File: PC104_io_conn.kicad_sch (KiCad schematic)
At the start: 14 parts, among them J13 ESQ-126-39-G-D_SAI, J15 ESQ-126-39-G-D_SAI

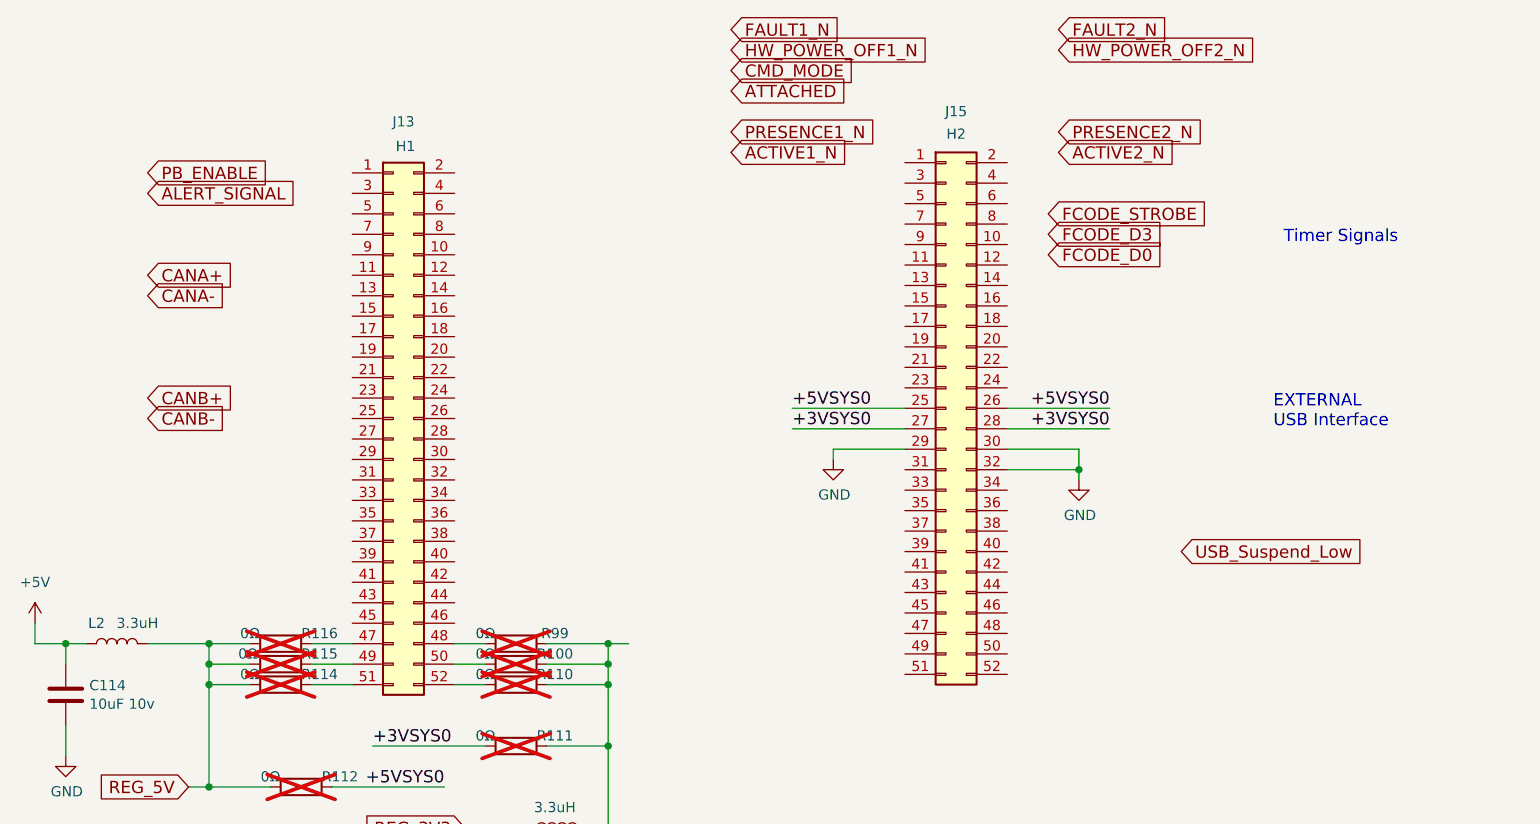
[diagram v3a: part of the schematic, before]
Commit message: Finish up temporary PC104 assignments
Finish up most of what is required for the CubeSat Kit Bus conversion.

Signed-off-by: Corey Minyard <corey@minyard.net>
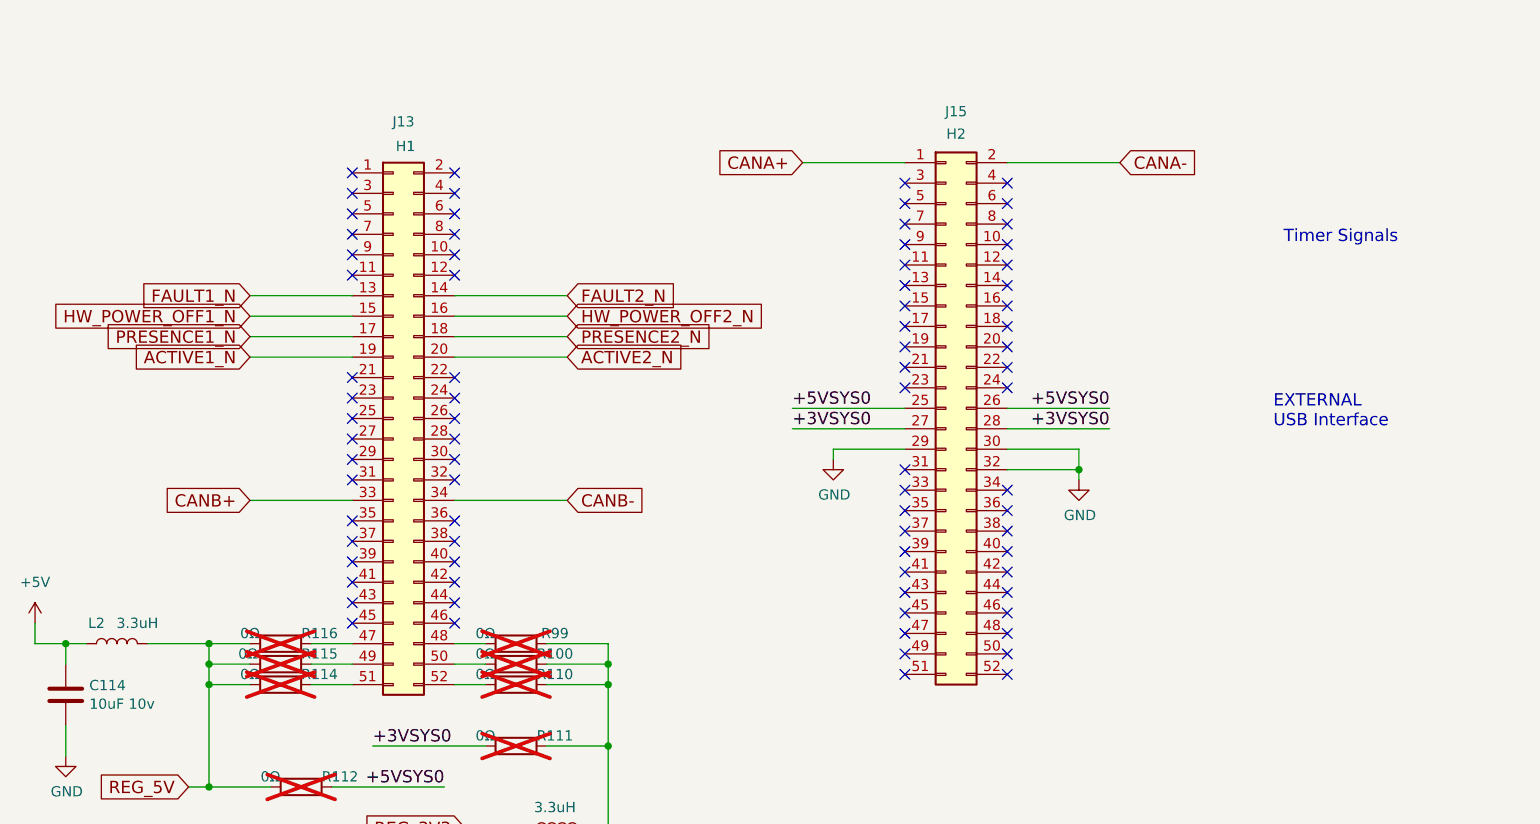
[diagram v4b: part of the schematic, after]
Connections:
- net ACTIVE1_N: now also J13.19 (Pin_19)
- net ACTIVE2_N: now also J13.20 (Pin_20)
- net CANA+: now also J15.1 (Pin_1)
- net CANA-: now also J15.2 (Pin_2)
- net CANB+: now also J13.33 (Pin_33)
- net CANB-: now also J13.34 (Pin_34)
- net FAULT1_N: now also J13.13 (Pin_13)
- net FAULT2_N: now also J13.14 (Pin_14)
- net HW_POWER_OFF1_N: now also J13.15 (Pin_15)
- net HW_POWER_OFF2_N: now also J13.16 (Pin_16)
- net PRESENCE1_N: now also J13.17 (Pin_17)
- net PRESENCE2_N: now also J13.18 (Pin_18)
- no-connect marks 0 -> 79

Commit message: Minor fixes for BOM values
Signed-off-by: Corey Minyard <corey@minyard.net>
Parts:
- R115: value 0Ω' -> 0Ω
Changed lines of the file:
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@@
 			)
 		)
-		(property "Value" "0Ω'"
+		(property "Value" "0Ω"
 			(at 125.73 156.21 90)
 			(effects

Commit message: Added some docs and notes about various things
Signed-off-by: Corey Minyard <corey@minyard.net>
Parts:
- R100, R110, R111, R112, R114, R115, R116, R99: now left out of the parts list
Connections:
- net 3V3_S1: now reaches J13.48 (Pin_48), R99.1
- net 5V_S2: now reaches J13.49 (Pin_49), R115.2
- net 5V_S1: now reaches J13.47 (Pin_47), R116.2
- net 3V3_S2: now reaches J13.50 (Pin_50), R100.1
- net 5V_S3: now reaches J13.51 (Pin_51), R114.2
- net 3V3_S3: now reaches J13.52 (Pin_52), R110.1
- net +3VSYS0 renamed 3V3_p
- net +5VSYS0 renamed 5V_p
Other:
- moved on the sheet: C114, C133, L2, L29, R100, R110, R111, R112, R114, R115, R116, R99

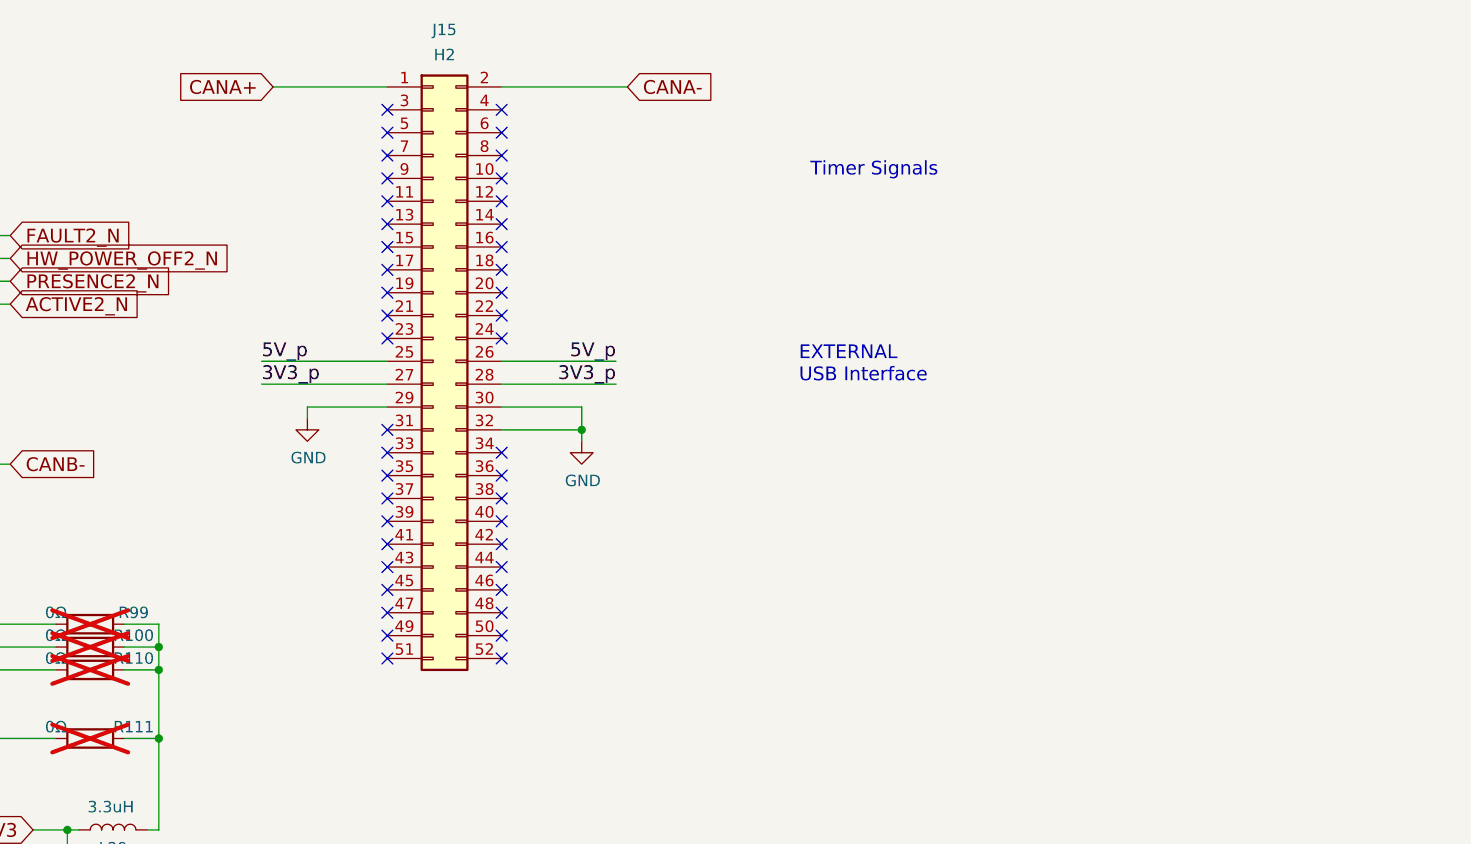
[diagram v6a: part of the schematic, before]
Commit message: Add an UMBILICAL_ATTACHED signal from the PC104
Allow the board to know if it is in the launch vehicle.  Will
hardware inhibit transmit.

Signed-off-by: Corey Minyard <corey@minyard.net>
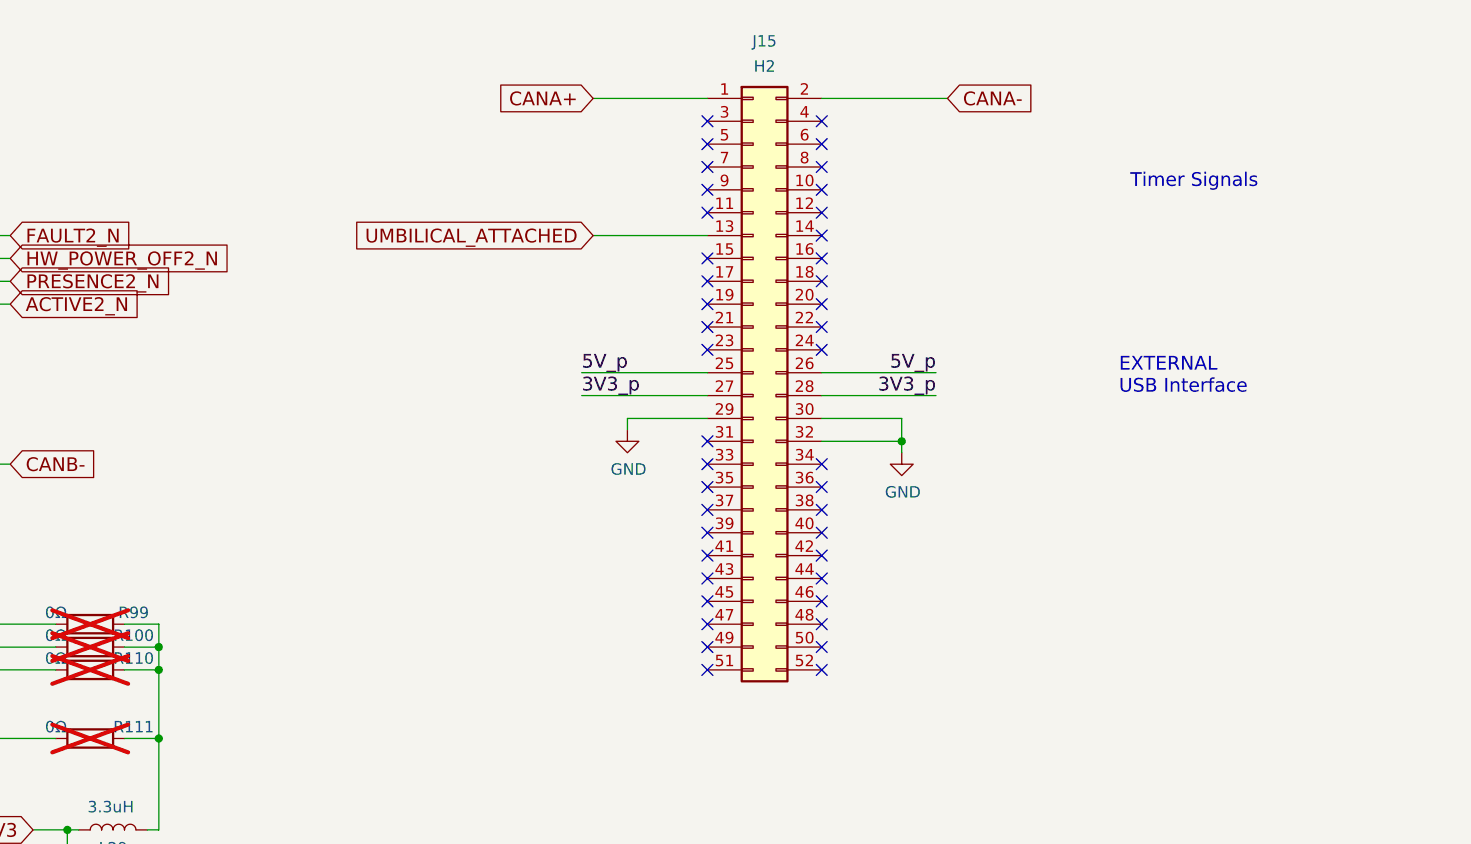
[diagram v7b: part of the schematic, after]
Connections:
- net UMBILICAL_ATTACHED: now reaches J15.13 (Pin_13)
- no-connect marks 79 -> 78
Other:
- moved on the sheet: J15

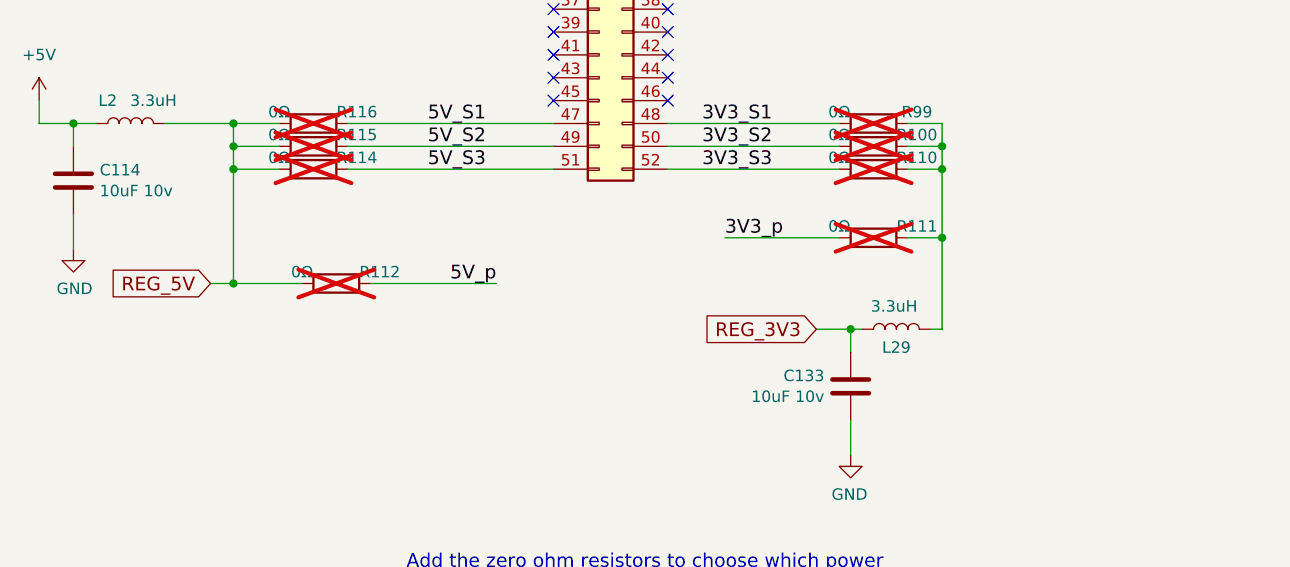
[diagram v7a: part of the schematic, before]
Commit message: Move 3.3V bench input to the other side of the inductor
Signed-off-by: Corey Minyard <corey@minyard.net>
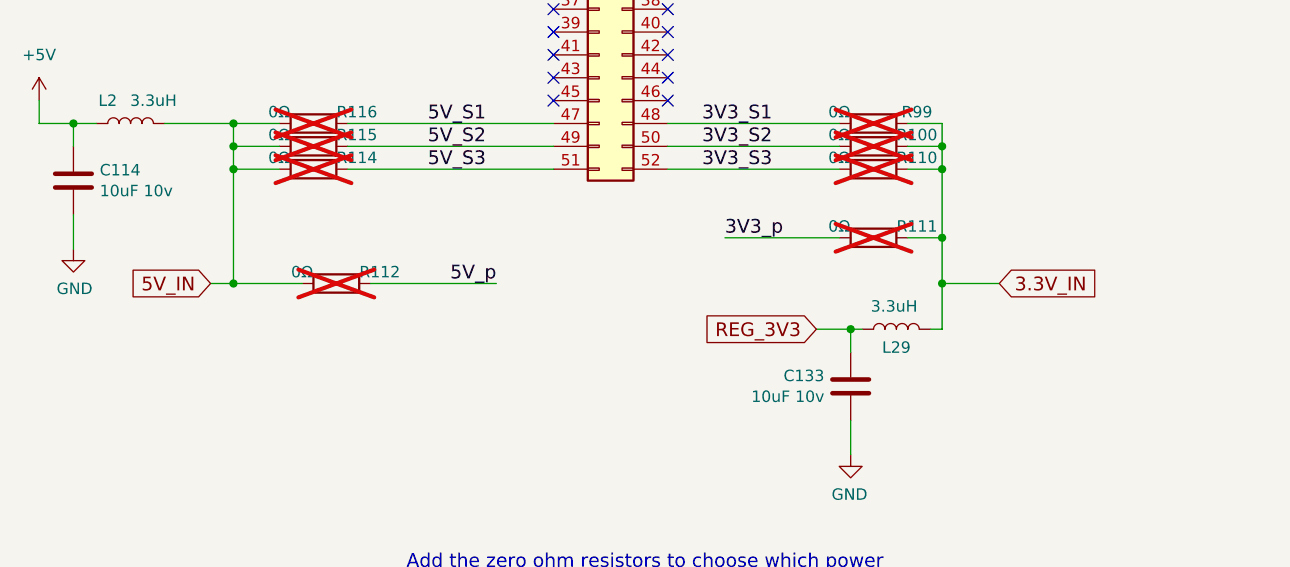
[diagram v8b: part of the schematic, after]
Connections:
- net 3.3V_IN: now reaches L29.1, R100.2, R110.2, R111.2, R99.2
- net REG_5V renamed 5V_IN
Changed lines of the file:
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@@
+	)
+	(junction
+		(at 181.61 172.72)
+		(diameter 0)
+		(color 0 0 0 0)
 	)
 	(junction
@@
 	(wire
 		(pts
-			(xy 181.61 167.64) (xy 181.61 177.8)
+			(xy 181.61 167.64) (xy 181.61 172.72)
 		)
 		(stroke
@@
 	(wire
 		(pts
+			(xy 181.61 172.72) (xy 187.96 172.72)
+		)
+		(stroke
+			(width 0)
+			(type default)
+		)
+	)
+	(wire
+		(pts
 			(xy 181.61 157.48) (xy 181.61 154.94)
 		)
@@
 		(pts
 			(xy 151.13 119.38) (xy 165.1 119.38)
+		)
+		(stroke
+			(width 0)
+			(type default)
+		)
+	)
+	(wire
+		(pts
+			(xy 181.61 172.72) (xy 181.61 177.8)
 		)
 		(stroke
@@
 		)
 	)
-	(global_label "REG_5V"
+	(global_label "3.3V_IN"
+		(shape input)
+		(at 187.96 172.72 0)
+		(fields_autoplaced yes)
+		(effects
+			(font
+				(size 1.524 1.524)
+			)
+			(justify left)
+		)
+		(property "Intersheetrefs" "${INTERSHEET_REFS}"
+			(at 199.175 172.72 0)
+			(effects
+				(font
+					(size 1.27 1.27)
+				)
+				(justify left)
+				(hide yes)
+			)
+		)
+	)
+	(global_label "5V_IN"
 		(shape input)
 		(at 100.33 172.72 180)
